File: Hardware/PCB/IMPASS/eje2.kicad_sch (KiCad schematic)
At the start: 18 parts, among them Q10 BC847BDW1, Q11 DMN3008SFG, Q12 DMN3008SFG, Q13 DMP3013SFV, Q14 DMP3013SFV, Q15 DMN3008SFG, Q16 DMN3008SFG, Q7 BC847BDW1, Q8 DMP3013SFV, Q9 DMP3013SFV

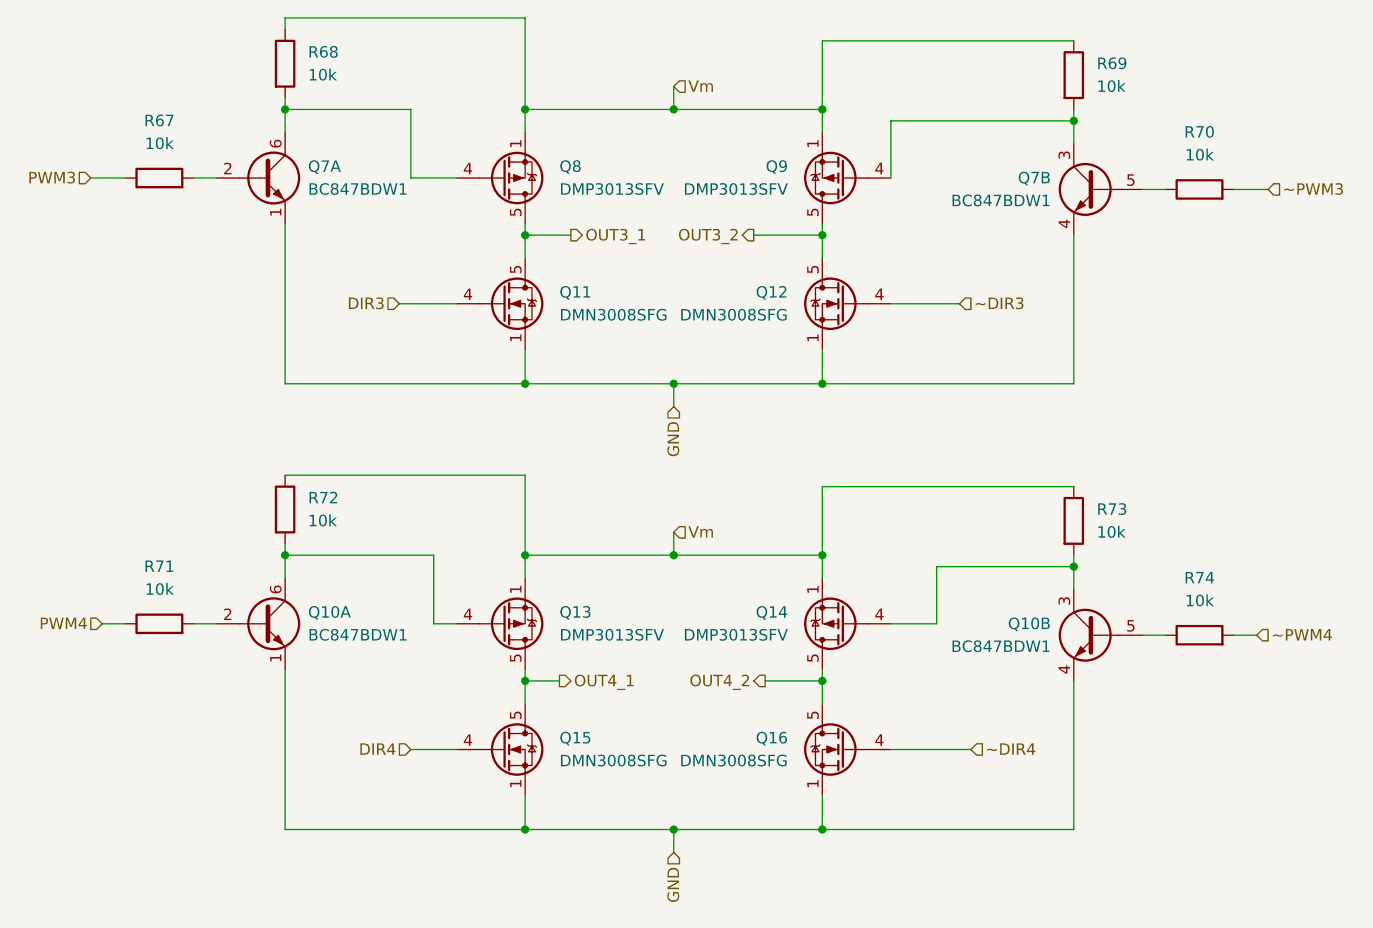
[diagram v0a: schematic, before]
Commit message: Hardware: Update all the logic pcb 	- added ads1015 	- added the logic foe P-MOSFET 	- added I2C connector
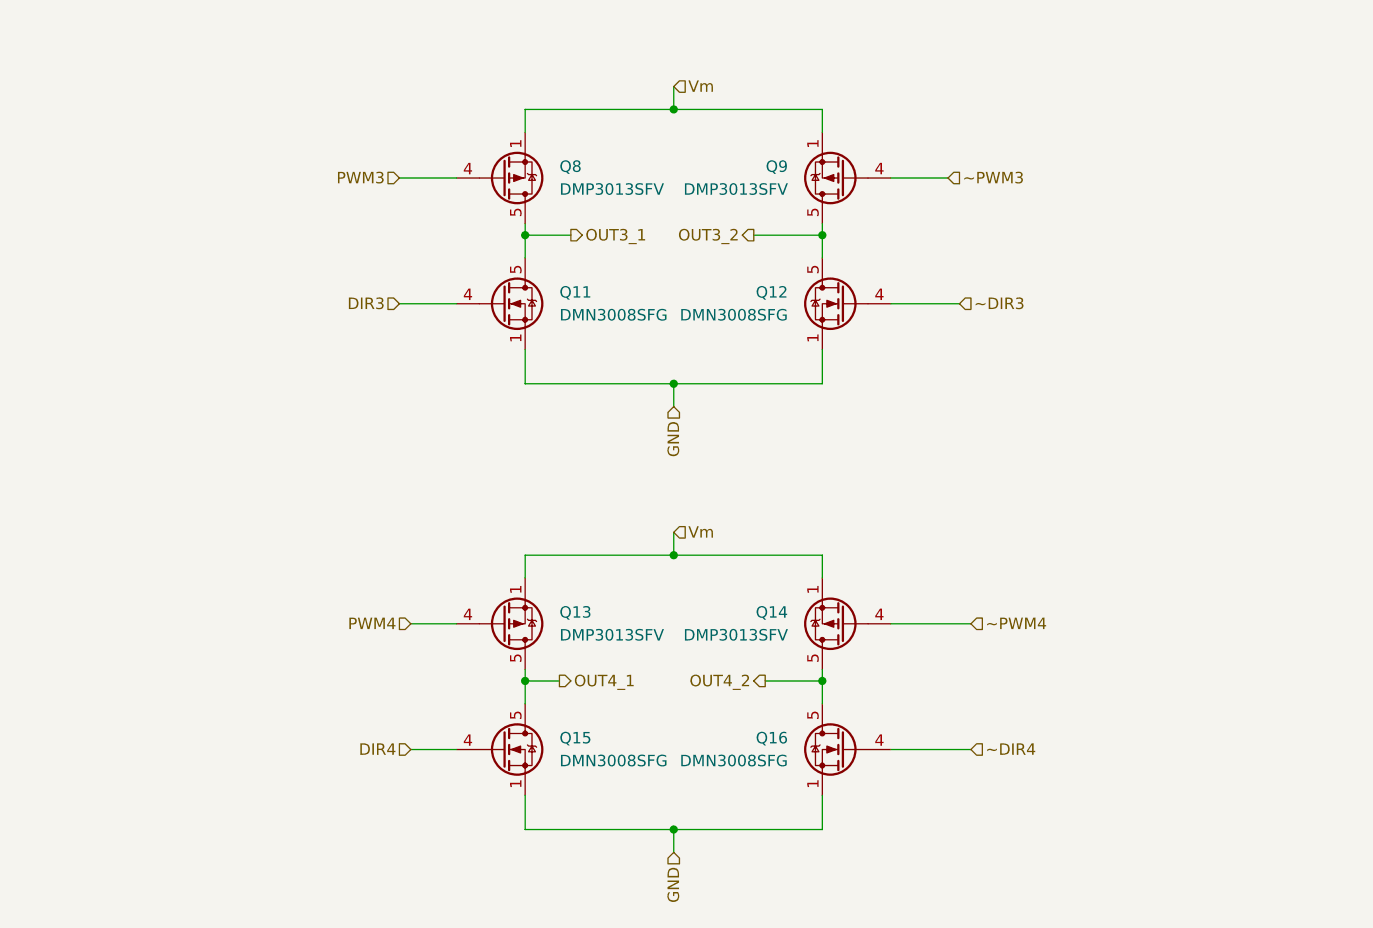
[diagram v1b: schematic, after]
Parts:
- removed Q10, Q7: BC847BDW1, Package_TO_SOT_SMD:SOT-363_SC-70-6, symbol Transistor_BJT:BC847BDW1
- removed R67, R68, R69, R70, R71, R72, R73, R74: 10k, Resistor_SMD:R_0603_1608Metric, symbol Device:R
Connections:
- net PWM3: now also Q8.4 (G)
- net PWM4: now also Q13.4 (G)
- net ~PWM3: now also Q9.4 (G)
- net ~PWM4: now also Q14.4 (G)
